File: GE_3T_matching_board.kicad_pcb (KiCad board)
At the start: 2 copper layers, 18.5 x 9.5 mm, 7 parts

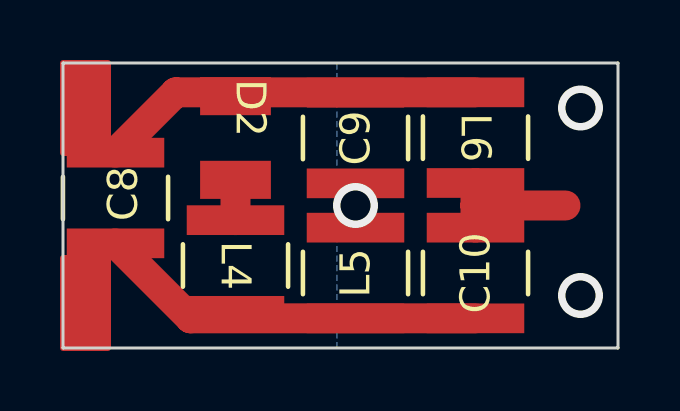
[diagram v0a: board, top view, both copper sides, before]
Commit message: added solder paste for coil terminals, smaller bottom copper
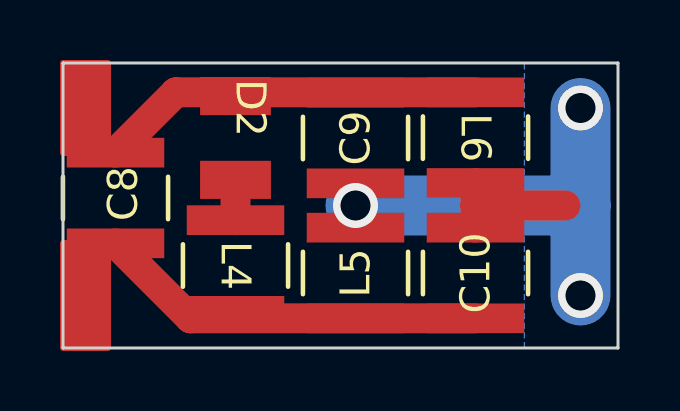
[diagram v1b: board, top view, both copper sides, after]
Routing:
- net GND: track 0.00 -> 13.8 mm
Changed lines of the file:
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@@
   (gr_rect (start 111.25 101.25) (end 112.75 104.25)
     (stroke (width 0.2) (type solid)) (fill solid) (layer "F.Cu"))
-  (gr_rect (start 111.25 107.75) (end 112.75 110.75)
+  (gr_rect (start 111.25 107.25) (end 112.75 110.75)
     (stroke (width 0.2) (type solid)) (fill solid) (layer "F.Cu"))
+  (gr_rect (start 111.25 107.25) (end 112.75 110.75)
+    (stroke (width 0.15) (type solid)) (fill solid) (layer "F.Paste"))
+  (gr_rect (start 111.25 101.25) (end 112.75 104.25)
+    (stroke (width 0.15) (type solid)) (fill solid) (layer "F.Paste"))
+  (gr_rect (start 111.25 107.25) (end 112.75 110.75)
+    (stroke (width 0.15) (type solid)) (fill solid) (layer "F.Mask"))
+  (gr_rect (start 111.25 101.25) (end 112.75 104.25)
+    (stroke (width 0.15) (type solid)) (fill solid) (layer "F.Mask"))
   (gr_line (start 111.25 110.75) (end 111.25 101.25)
     (stroke (width 0.1) (type default)) (layer "Edge.Cuts"))
@@
   (via (at 128.5 109) (size 1.5) (drill 1) (layers "F.Cu" "B.Cu") (net 1))
   (via (at 128.5 102.75) (size 1.5) (drill 1) (layers "F.Cu" "B.Cu") (net 1))
+  (segment (start 121 106) (end 128.5 106) (width 2) (layer "B.Cu") (net 1))
+  (segment (start 128.5 102.75) (end 128.5 109) (width 2) (layer "B.Cu") (net 1))
   (segment (start 125 102.2274) (end 115.0113 102.2274) (width 1) (layer "F.Cu") (net 2))
   (segment (start 115.0113 102.2274) (end 113 104.2387) (width 1) (layer "F.Cu") (net 2))
@@
     (polygon
       (pts
-        (xy 120.38 101.25)
+        (xy 126.63 101.25)
         (xy 129.76 101.25)
         (xy 129.76 110.75)
-        (xy 120.38 110.75)
+        (xy 126.63 110.75)
       )
     )
